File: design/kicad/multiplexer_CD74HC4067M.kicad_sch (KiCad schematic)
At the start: 7 parts, among them U1 CD74HC4067M

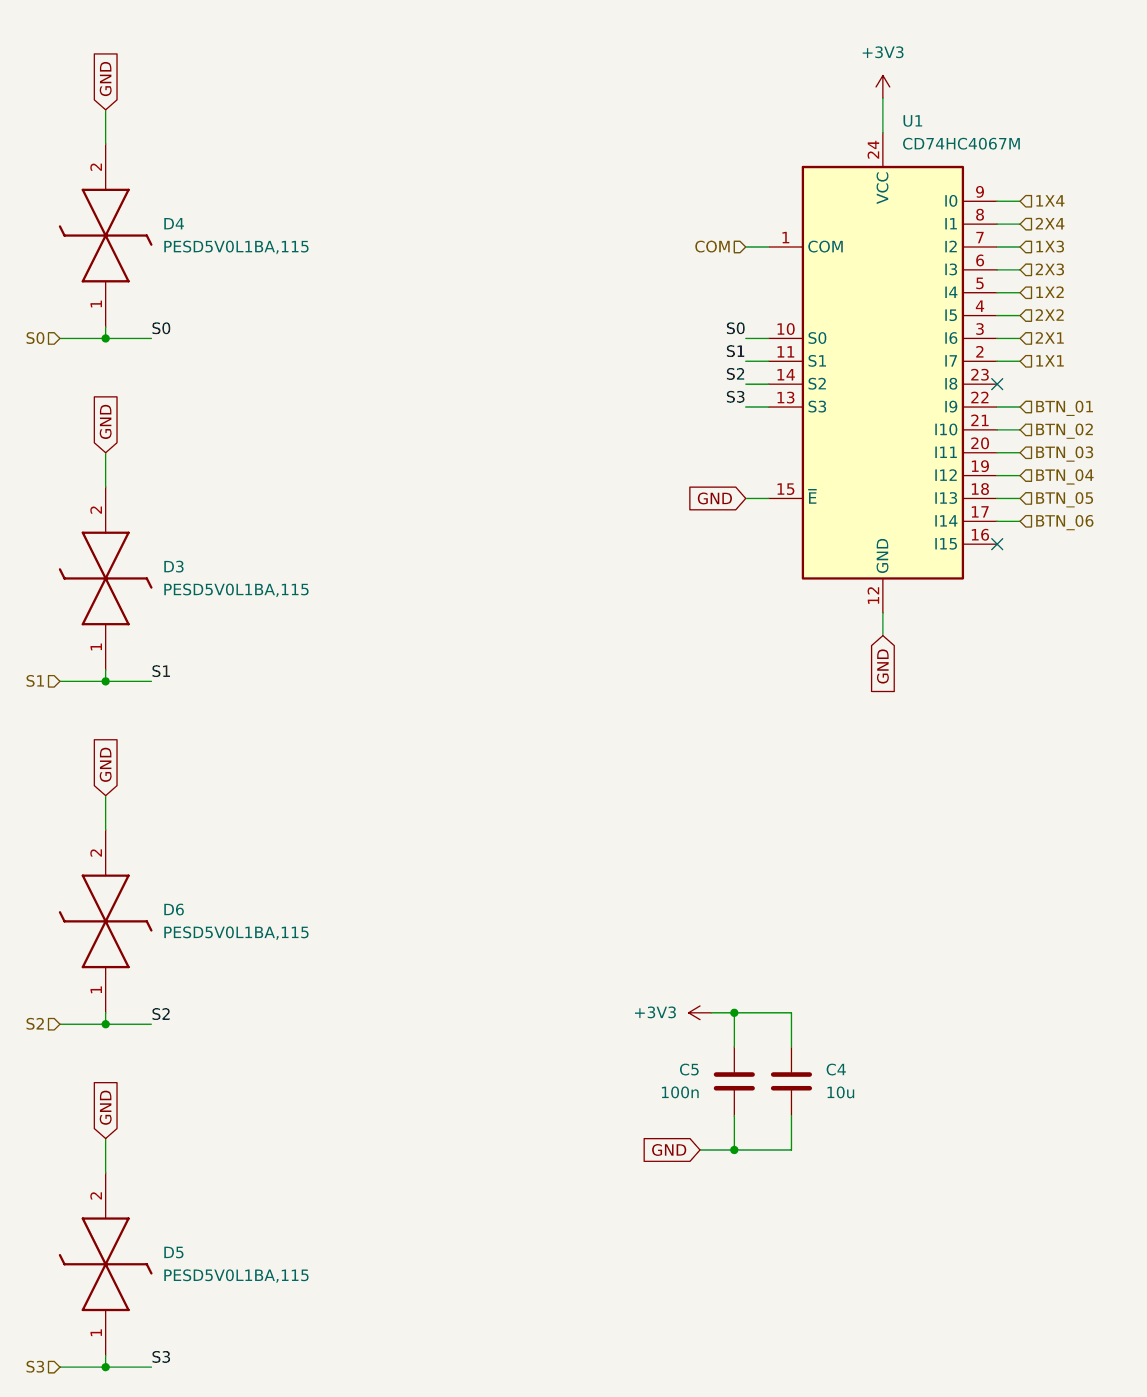
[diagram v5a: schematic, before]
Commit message: Update kicad binary files
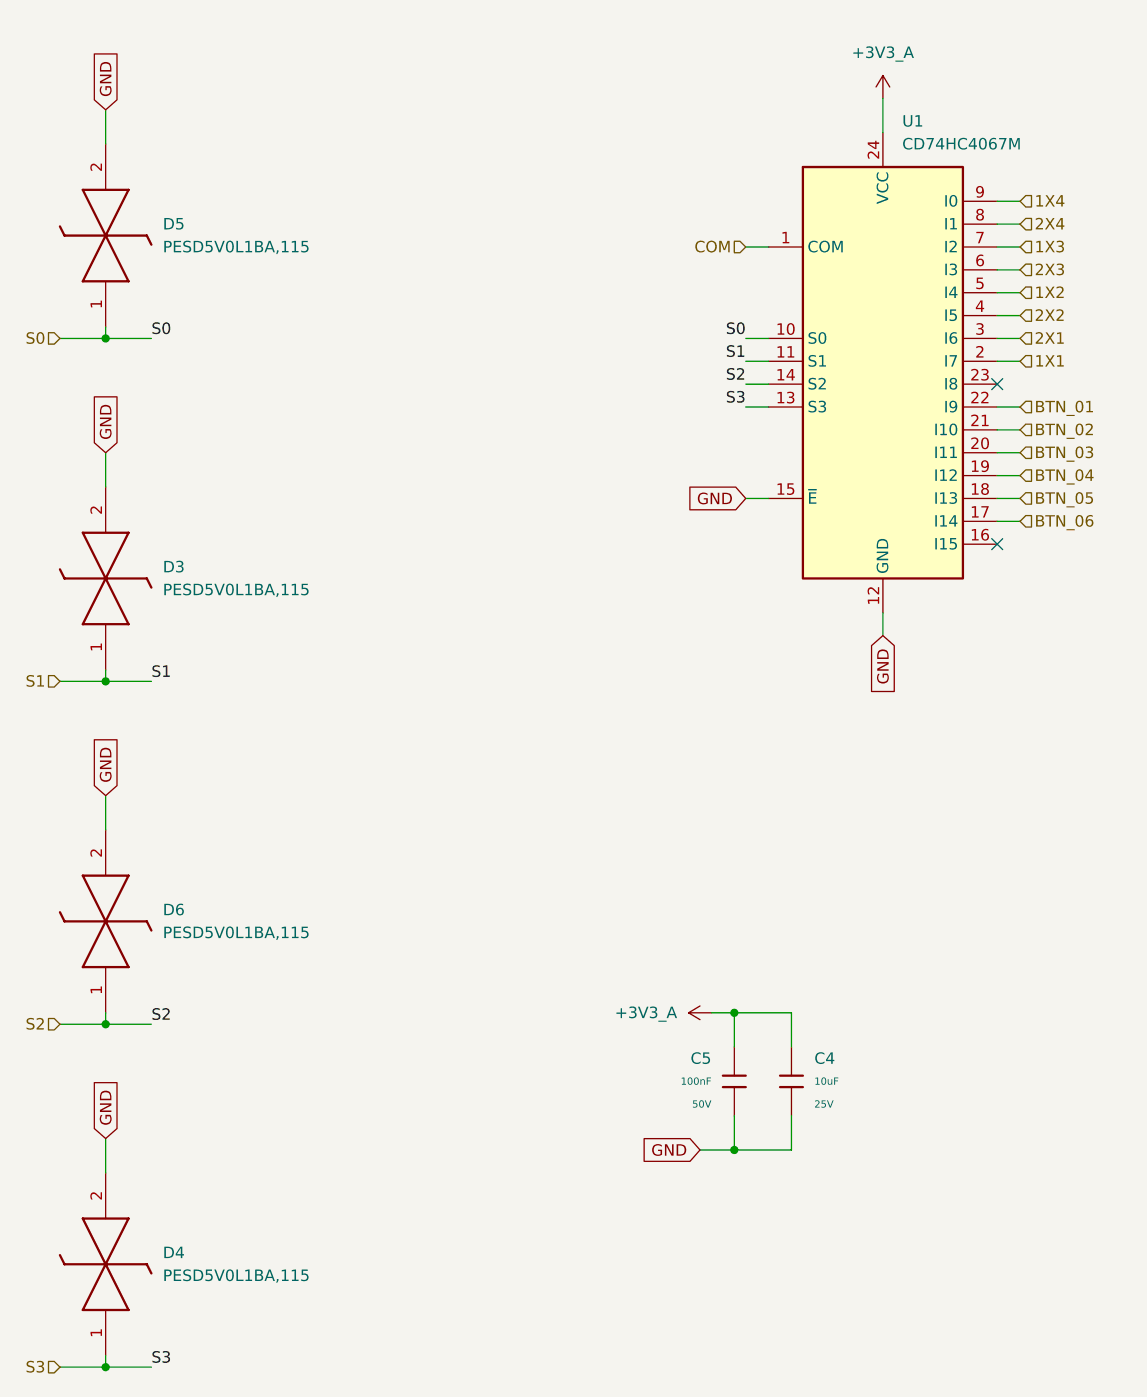
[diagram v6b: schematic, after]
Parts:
- removed C4: 10u, Capacitor_SMD:C_0805_2012Metric, symbol Device:C
- removed C5: 100n, Capacitor_SMD:C_0603_1608Metric, symbol Device:C
- added C4: 10uF, PCM_JLCPCB:C_0805, symbol PCM_JLCPCB-Capacitors:0805,10uF
- added C5: 100nF, PCM_JLCPCB:C_0603, symbol PCM_JLCPCB-Capacitors:0603,100nF
- renumbered D5 to D4, D4 to D5
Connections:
- net GND: now also C4.2, C5.2
- net +3V3 renamed +3V3_A
- net +3V3_A: now also C4.1, C5.1
